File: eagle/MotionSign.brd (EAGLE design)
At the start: 85.9 x 47.6 mm, 77 parts, among them Q1 16MHZ, U1 ATMEGA328, U2 L7805CDT-TR, U3 NCS36000, U4 PIR, U5 WS2801, U6 SPX3819, U7 NJVMJD2955T4G, U8 TXB0108PWR, U9 LCD-HD4478020X4-4HOLES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

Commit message: Swap out power managment resistor with 204/7 for
Allow for further experimentation with power managment
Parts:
- R15: device MotionSign:M0805 -> MotionSign:0204/7
- moved R15 1.37 mm to (100.3, 13.6)
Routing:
- net L7805_IN: track 16.1 -> 14.6 mm
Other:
- board text added: "MOTION?"
- board text added: "OCCUPIED?"
- board text added: "POWER?"
- board text added: "RESERVED?"
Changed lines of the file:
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@@
 <text x="103.378" y="17.272" size="1.016" layer="26" rot="MR0" align="bottom-center">&lt;-InTentss=Designs-&gt;
 ||-MotionSign V1-||</text>
+<text x="46.99" y="19.304" size="0.508" layer="25" rot="R90" align="bottom-center">OCCUPIED?</text>
+<text x="70.358" y="44.704" size="0.508" layer="25" align="bottom-center">RESERVED?</text>
+<text x="121.92" y="8.382" size="0.508" layer="26" rot="MR0" align="bottom-center">POWER?</text>
+<text x="124.46" y="28.448" size="0.508" layer="26" rot="MR270" align="bottom-center">MOTION?</text>
+<text x="45.72" y="10.668" size="0.508" layer="21" font="vector" ratio="12" rot="R90" align="bottom-center">GND</text>
+<text x="45.72" y="16.002" size="0.508" layer="21" font="vector" ratio="12" rot="R90" align="bottom-center">V+</text>
+<text x="45.72" y="18.288" size="0.508" layer="21" font="vector" ratio="12" rot="R90" align="bottom-center">RX</text>
+<text x="45.72" y="20.828" size="0.508" layer="21" font="vector" ratio="12" rot="R90" align="bottom-center">TX</text>
+<text x="45.72" y="20.828" size="0.508" layer="22" font="vector" ratio="12" rot="MR270" align="bottom-center">TX</text>
+<text x="45.72" y="18.288" size="0.508" layer="22" font="vector" ratio="12" rot="MR270" align="bottom-center">RX</text>
+<text x="45.72" y="16.002" size="0.508" layer="22" font="vector" ratio="12" rot="MR270" align="bottom-center">V+</text>
+<text x="45.72" y="10.668" size="0.508" layer="22" font="vector" ratio="12" rot="MR270" align="bottom-center">GND</text>
 </plain>
 <attributes>
@@
 <element name="U$1" library="MotionSign" library_urn="urn:adsk.eagle:library:3048452" package="LENS-CWM-0.5-GI-V1" package3d_urn="urn:adsk.eagle:package:3049104/1" value="CWM 0.5 GI V1" x="109.22" y="32.639" rot="MR0"/>
 <element name="D1" library="led" library_urn="urn:adsk.eagle:library:259" package="CHIPLED_0805" package3d_urn="urn:adsk.eagle:package:15821/2" value="Green" x="125.476" y="27.813" smashed="yes" rot="MR0">
-<attribute name="NAME" x="124.46" y="26.797" size="0.508" layer="26" rot="MR270" align="bottom-center"/>
+<attribute name="NAME" x="124.46" y="26.035" size="0.508" layer="26" rot="MR270" align="bottom-center"/>
 <attribute name="VALUE" x="123.952" y="28.321" size="0.508" layer="28" rot="MR90" align="bottom-center"/>
 </element>
@@
 <attribute name="VALUE" x="98.044" y="18.65" size="0.508" layer="27" rot="R90"/>
 </element>
-<element name="R15" library="MotionSign" library_urn="urn:adsk.eagle:library:3048452" package="M0805" package3d_urn="urn:adsk.eagle:package:3049036/2" value="22" x="101.6" y="14.097" smashed="yes">
-<attribute name="NAME" x="99.822" y="13.589" size="0.508" layer="25" rot="R90"/>
-<attribute name="VALUE" x="103.886" y="13.589" size="0.508" layer="27" rot="R90"/>
+<element name="R15" library="MotionSign" library_urn="urn:adsk.eagle:library:3048452" package="0204/7" package3d_urn="urn:adsk.eagle:package:3048939/2" value="22" x="100.33" y="13.589" smashed="yes">
+<attribute name="NAME" x="98.552" y="13.081" size="0.508" layer="25" rot="R90"/>
+<attribute name="VALUE" x="102.616" y="13.081" size="0.508" layer="27" rot="R90"/>
 </element>
 <element name="S3" library="MotionSign" library_urn="urn:adsk.eagle:library:3048452" package="TACTILE_SWITCH_SMD_5.2MM" package3d_urn="urn:adsk.eagle:package:3048933/2" value="Reset" x="76.708" y="7.62" smashed="yes" rot="R270">
@@
 <wire x1="113.046" y1="15.494" x2="105.174" y2="15.494" width="0.762" layer="1"/>
 <wire x1="105.174" y1="15.494" x2="103.88" y2="16.788" width="0.762" layer="1"/>
-<wire x1="103.88" y1="16.788" x2="103.88" y2="15.427" width="0.762" layer="1"/>
-<wire x1="103.88" y1="15.427" x2="102.55" y2="14.097" width="0.762" layer="1"/>
 <contactref element="JP2" pad="1"/>
-<wire x1="108.3564" y1="15.24" x2="108.6104" y2="15.494" width="0.508" layer="16"/>
+<wire x1="108.3564" y1="15.24" x2="108.6104" y2="15.494" width="0.254" layer="16"/>
 <wire x1="108.6104" y1="15.494" x2="113.046" y2="15.494" width="0.762" layer="16"/>
+<wire x1="104.14" y1="13.589" x2="103.88" y2="13.849" width="0.762" layer="1"/>
+<wire x1="103.88" y1="13.849" x2="103.88" y2="16.788" width="0.762" layer="1"/>
 </signal>
 <signal name="A5">
@@
 <wire x1="116.967" y1="13.335" x2="118.618" y2="12.192" width="0.254" layer="1"/>
 <wire x1="114.554" y1="13.335" x2="116.967" y2="13.335" width="0.254" layer="1"/>
-<wire x1="114.046" y1="12.827" x2="114.554" y2="13.335" width="0.254" layer="1"/>
-<wire x1="99.822" y1="12.827" x2="114.046" y2="12.827" width="0.254" layer="1"/>
-<wire x1="98.933" y1="13.716" x2="99.822" y2="12.827" width="0.254" layer="1"/>
-<wire x1="98.933" y1="22.479" x2="98.933" y2="13.716" width="0.254" layer="16"/>
+<wire x1="98.933" y1="22.479" x2="98.933" y2="13.97" width="0.254" layer="16"/>
 <wire x1="89.027" y1="32.385" x2="98.933" y2="22.479" width="0.254" layer="16"/>
 <wire x1="89.027" y1="34.798" x2="89.027" y2="32.385" width="0.254" layer="16"/>
@@
 <wire x1="121.793" y1="21.717" x2="121.672" y2="21.717" width="0.254" layer="1"/>
 <wire x1="89.662" y1="36.195" x2="89.67816875" y2="36.28048125" width="0.254" layer="1"/>
-<via x="98.933" y="13.716" extent="1-16" drill="0.381"/>
+<via x="98.933" y="13.97" extent="1-16" drill="0.381"/>
 <via x="89.027" y="34.798" extent="1-16" drill="0.381"/>
+<wire x1="98.933" y1="13.97" x2="100.076" y2="12.827" width="0.254" layer="1"/>
+<wire x1="100.076" y1="12.827" x2="103.1777875" y2="12.827" width="0.254" layer="1"/>
+<wire x1="103.1777875" y1="12.827" x2="103.6349875" y2="12.3698" width="0.254" layer="1"/>
+<wire x1="103.6349875" y1="12.3698" x2="113.5888" y2="12.3698" width="0.254" layer="1"/>
+<wire x1="113.5888" y1="12.3698" x2="114.554" y2="13.335" width="0.254" layer="1"/>
 </signal>
 <signal name="N$13">
@@
 <contactref element="R15" pad="1"/>
 <contactref element="U7" pad="1"/>
-<wire x1="100.65" y1="14.097" x2="100.1725" y2="14.5745" width="0.762" layer="1"/>
-<wire x1="100.1725" y1="14.5745" x2="99.32" y2="15.427" width="0.762" layer="1"/>
 <wire x1="99.32" y1="15.427" x2="99.32" y2="16.788" width="0.762" layer="1"/>
-<wire x1="90.684" y1="16.7245" x2="92.834" y2="14.5745" width="0.508" layer="1"/>
-<wire x1="92.834" y1="14.5745" x2="100.1725" y2="14.5745" width="0.508" layer="1"/>
 <wire x1="90.551" y1="16.51" x2="88.392" y2="16.51" width="0.508" layer="1"/>
 <wire x1="88.392" y1="16.51" x2="88.392" y2="16.422" width="0.508" layer="1"/>
 <wire x1="90.551" y1="16.51" x2="90.684" y2="16.7245" width="0.508" layer="1"/>
+<wire x1="96.52" y1="13.589" x2="93.8195" y2="13.589" width="0.508" layer="1"/>
+<wire x1="93.8195" y1="13.589" x2="90.684" y2="16.7245" width="0.508" layer="1"/>
+<wire x1="96.52" y1="13.589" x2="98.358" y2="15.427" width="0.762" layer="1"/>
+<wire x1="98.358" y1="15.427" x2="99.32" y2="15.427" width="0.762" layer="1"/>
 </signal>
 <signal name="RS_ESP">

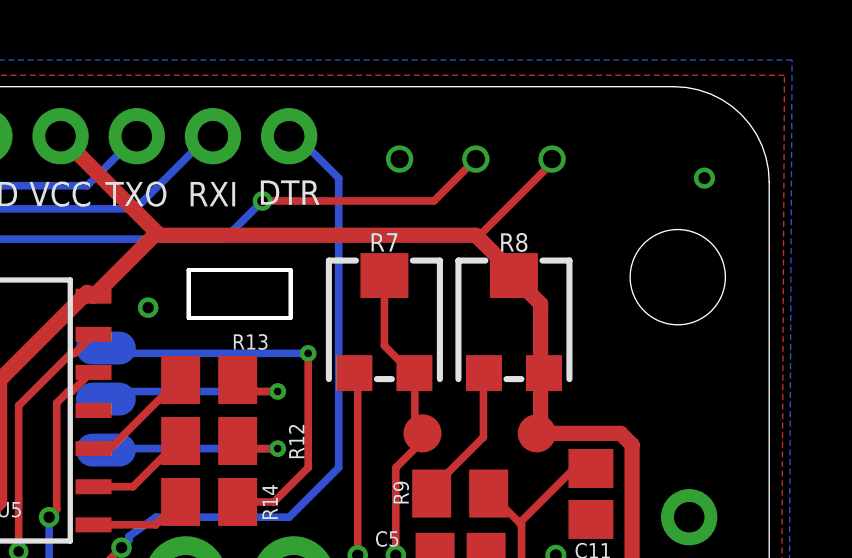
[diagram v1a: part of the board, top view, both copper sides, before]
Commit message: Add Sensitivity/Ossilation Names
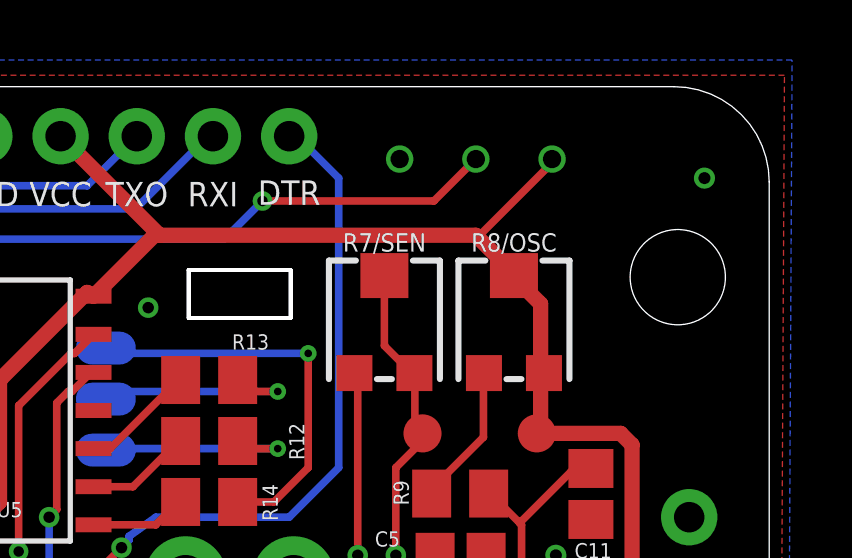
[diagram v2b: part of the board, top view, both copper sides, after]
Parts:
- renumbered R7 to R7/SEN, R8 to R8/OSC
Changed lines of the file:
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@@
 <attribute name="VALUE" x="112.483" y="27.8012" size="0.508" layer="27" rot="R90"/>
 </element>
-<element name="R7" library="MotionSign" library_urn="urn:adsk.eagle:library:3048452" package="TRIMPOT-TC33X" package3d_urn="urn:adsk.eagle:package:3049112/2" value="1M" x="114.046" y="43.053">
+<element name="R7/SEN" library="MotionSign" library_urn="urn:adsk.eagle:library:3048452" package="TRIMPOT-TC33X" package3d_urn="urn:adsk.eagle:package:3049112/2" value="1M" x="114.046" y="43.053">
 <attribute name="PROD_ID" value="RES-13431" x="81.534" y="23.241" size="1.778" layer="27" display="off"/>
 </element>
@@
 <attribute name="VALUE" x="120.1556" y="39.2938" size="0.508" layer="27"/>
 </element>
-<element name="R8" library="MotionSign" library_urn="urn:adsk.eagle:library:3048452" package="TRIMPOT-TC33X" package3d_urn="urn:adsk.eagle:package:3049112/2" value="1M" x="118.364" y="43.053">
+<element name="R8/OSC" library="MotionSign" library_urn="urn:adsk.eagle:library:3048452" package="TRIMPOT-TC33X" package3d_urn="urn:adsk.eagle:package:3049112/2" value="1M" x="118.364" y="43.053">
 <attribute name="PROD_ID" value="RES-13431" x="73.66" y="19.939" size="1.778" layer="27" display="off"/>
 </element>
@@
 <contactref element="ISP_V13" pad="4"/>
 <contactref element="U3" pad="14"/>
-<contactref element="R8" pad="2"/>
-<contactref element="R8" pad="3"/>
+<contactref element="R8/OSC" pad="2"/>
+<contactref element="R8/OSC" pad="3"/>
 <contactref element="TP2" pad="P$1"/>
 <contactref element="D1" pad="A"/>
@@
 <signal name="N$11">
 <contactref element="U3" pad="2"/>
-<contactref element="R7" pad="2"/>
+<contactref element="R7/SEN" pad="2"/>
 <contactref element="C9" pad="1"/>
 <contactref element="R4" pad="1"/>
-<contactref element="R7" pad="3"/>
+<contactref element="R7/SEN" pad="3"/>
 <contactref element="TP1" pad="P$1"/>
 <wire x1="115.062" y1="39.497" x2="115.062" y2="41.148" width="0.254" layer="1"/>
@@
 <signal name="N$13">
 <contactref element="R9" pad="2"/>
-<contactref element="R8" pad="1"/>
+<contactref element="R8/OSC" pad="1"/>
 <wire x1="117.348" y1="39.116" x2="117.348" y2="41.148" width="0.254" layer="1"/>
 <wire x1="115.57" y1="37.338" x2="117.348" y2="39.116" width="0.254" layer="1"/>
@@
 <contactref element="C9" pad="2"/>
 <contactref element="U3" pad="1"/>
-<contactref element="R7" pad="1"/>
+<contactref element="R7/SEN" pad="1"/>
 <contactref element="U1" pad="23"/>
 <wire x1="115.189" y1="29.337" x2="116.072" y2="29.337" width="0.254" layer="1"/>

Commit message: Add door reed switch
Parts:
- removed C19: 0.33uF, MotionSign:C0805
- removed JP2: USE 5V POWER, MotionSign:SMT-JUMPER_2_NO_SILK
- removed R15: 22, MotionSign:0204/7
- removed U2: L7805CDT-TR, MotionSign:DPAK
- removed U7: NJVMJD2955T4G, MotionSign:DPAK
- added DOOR: (no value), MotionSign:JST-2-PTH
- R11: value 300 -> 1k
- R18, R19, R2, R20, R21, R22: value 10K -> 10k
- R23: value 1K -> 1k
- moved S4 49.4 mm to (99.6, 15.7), flipped to the bottom, turned to 90 degrees
- moved S3 32.1 mm to (107.7, 16.0), flipped to the bottom, turned to 90 degrees
- moved R19 31.3 mm to (76.5, 11.4), turned to 0 degrees
- moved LEDS 0.76 mm to (101.9, 9.40)
- moved JP4 0.51 mm to (127.3, 15.5)
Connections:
- removed net D2: U1.32
- removed net L7805_IN: C19.1, R15.1, U2.1, U7.1
- removed net RAW: JP2.1, JP4.PWR, R15.2, U7.3
- new net DOOR: DOOR.2, U1.32
- net GND: now also DOOR.1; no longer C19.2, U2.4
- net VCC: now also JP4.PWR; no longer JP2.2, U2.3, U7.4
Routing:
- net DOOR: track 0.00 -> 41.0 mm, vias 0 -> 1
- net GPIO0: track 26.5 -> 56.1 mm, vias 2 -> 3
- net RAW: track 17.8 -> 0.00 mm
- net L7805_IN: track 14.6 -> 0.00 mm
- net RESET_HZA: track 38.7 -> 45.3 mm, vias 2 -> 4
- net 3.3V: track 70.2 -> 66.3 mm
- net OUT: track 60.6 -> 62.5 mm
- net VCC: track 285.0 -> 283.2 mm
- net SD0: track 33.2 -> 34.1 mm
- net GND: track 1.09 -> 1.83 mm
- net LCD_E: track 18.8 -> 18.3 mm
- net N$20: track 14.1 -> 13.5 mm
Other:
- board text added: "MotionSign V1"
- board text added: "VCC: 5V"
- board text removed: "MAX: 1.5A"
- board text removed: "MotionSign V0"
- board text removed: "VCC: 9-12V"
